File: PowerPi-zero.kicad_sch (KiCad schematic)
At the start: 34 parts, among them J1 2444, J3 Conn_01x02, J6 Raspberry_Pi_2_3, J8 2444, Q1 30V 4A 44mΩ, Q2 50nA 150V 200mW 200mA, Q3 30V 4A 44mΩ, U1 XL4015

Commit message: Layout complete for PowerPi zero
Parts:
- removed D2: SS54, Diode_SMD:D_SMA, symbol Device:D_Schottky
- removed H5, H6, H7, H8: MountingHole, MountingHole:MountingHole_3.5mm, symbol Mechanical:MountingHole
- removed J3: Conn_01x02, Connector_JST:JST_XH_B2B-XH-A_1x02_P2.50mm_Vertical, symbol Connector_Generic:Conn_01x02
- removed JP1: SolderJumper_3_Bridged12, Jumper:SolderJumper-3_P1.3mm_Bridged2Bar12_RoundedPad1.0x1.5mm, symbol Jumper:SolderJumper_3_Bridged12

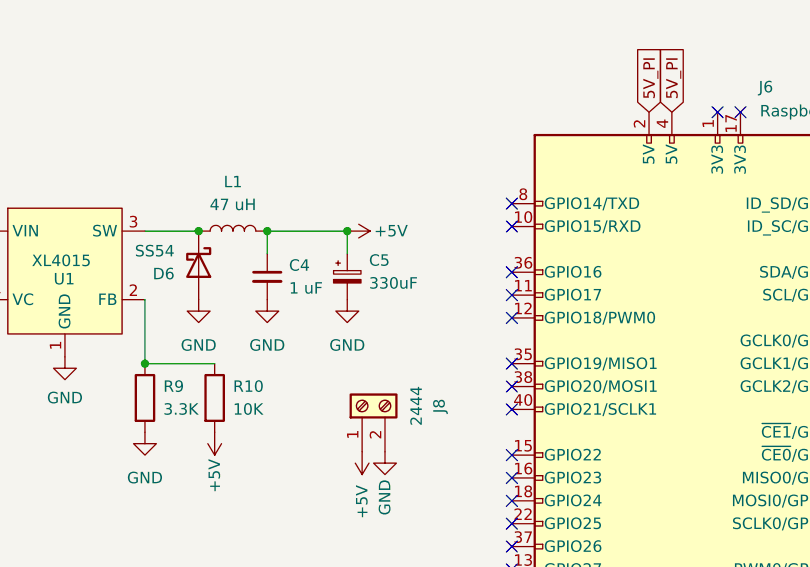
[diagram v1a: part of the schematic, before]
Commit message: update to 1000 uF output electrolytic capacitor
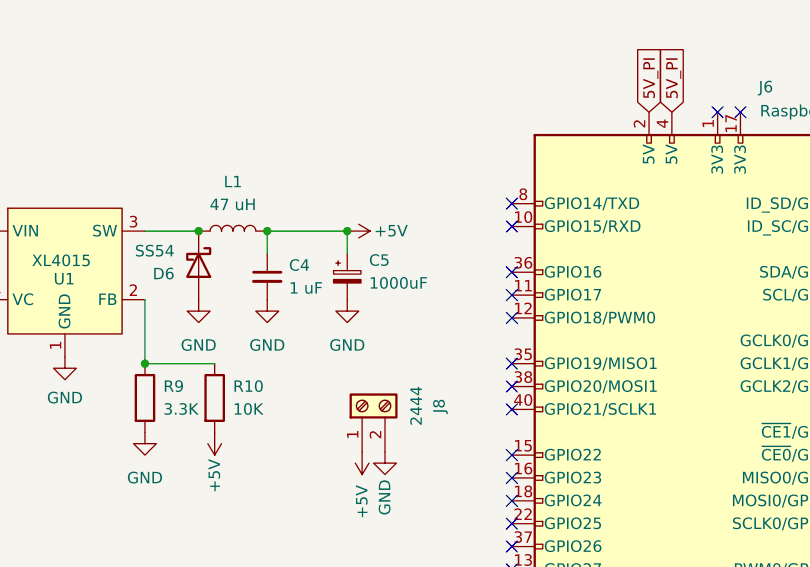
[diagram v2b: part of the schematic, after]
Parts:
- C5: value 330uF -> 1000uF; footprint Capacitor_SMD:CP_Elec_6.3x7.7 -> Capacitor_SMD:CP_Elec_8x10; LCSC C58277 -> C310838; ManfNum RVT1A331M0607 -> RVE1A102M0810; PCBway RVT1A331M0607 -> RVE1A102M0810; abv.Footprint SMD_6.3x7.7mm -> SMD_ECAP-8x10
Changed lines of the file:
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@@
       (effects (font (size 1.27 1.27)) (justify left))
     )
-    (property "Value" "330uF" (id 1) (at 126.111 101.4348 0)
-      (effects (font (size 1.27 1.27)) (justify left))
-    )
-    (property "Footprint" "Capacitor_SMD:CP_Elec_6.3x7.7" (id 2) (at 123.698 100.711 0)
+    (property "Value" "1000uF" (id 1) (at 126.111 101.4348 0)
+      (effects (font (size 1.27 1.27)) (justify left))
+    )
+    (property "Footprint" "Capacitor_SMD:CP_Elec_8x10" (id 2) (at 123.698 100.711 0)
       (effects (font (size 1.27 1.27)) hide)
     )
@@
       (effects (font (size 1.27 1.27)) hide)
     )
-    (property "LCSC" "C58277" (id 4) (at 123.698 100.711 0)
-      (effects (font (size 1.27 1.27)) hide)
-    )
-    (property "PCBway" "RVT1A331M0607" (id 5) (at 123.698 100.711 0)
-      (effects (font (size 1.27 1.27)) hide)
-    )
-    (property "abv.Footprint" "SMD_6.3x7.7mm" (id 6) (at 123.698 100.711 0)
-      (effects (font (size 1.27 1.27)) hide)
-    )
-    (property "ManfNum" "RVT1A331M0607" (id 7) (at 123.698 100.711 0)
+    (property "LCSC" "C310838" (id 4) (at 123.698 100.711 0)
+      (effects (font (size 1.27 1.27)) hide)
+    )
+    (property "PCBway" "RVE1A102M0810" (id 5) (at 123.698 100.711 0)
+      (effects (font (size 1.27 1.27)) hide)
+    )
+    (property "abv.Footprint" "SMD_ECAP-8x10" (id 6) (at 123.698 100.711 0)
+      (effects (font (size 1.27 1.27)) hide)
+    )
+    (property "ManfNum" "RVE1A102M0810" (id 7) (at 123.698 100.711 0)
       (effects (font (size 1.27 1.27)) hide)
     )
@@
     )
     (path "/858d080d-4b19-45cc-bb9f-d3c272f2a854"
-      (reference "C5") (unit 1) (value "330uF") (footprint "Capacitor_SMD:CP_Elec_6.3x7.7")
+      (reference "C5") (unit 1) (value "1000uF") (footprint "Capacitor_SMD:CP_Elec_8x10")
     )
     (path "/09682f05-b4e6-4e50-98a0-ce1e14e1d9ed"

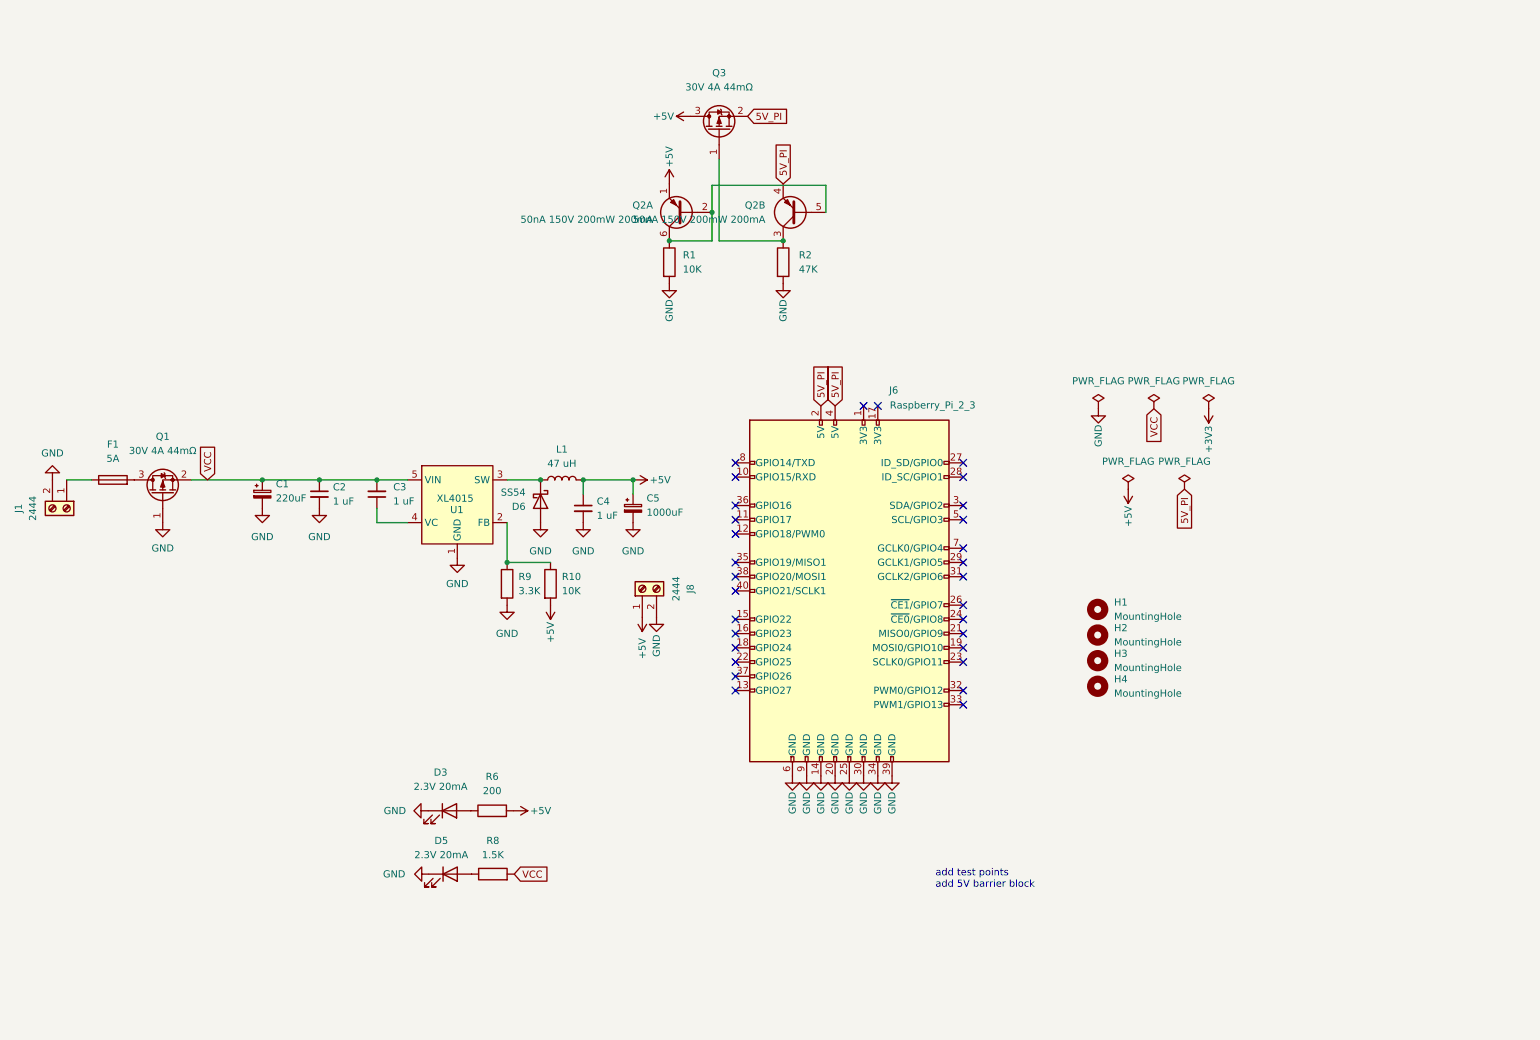
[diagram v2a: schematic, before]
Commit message: Brought full design up to date with ElectriPi
Main development was done on ElectriPi so now ElectriPi mini matches those developments
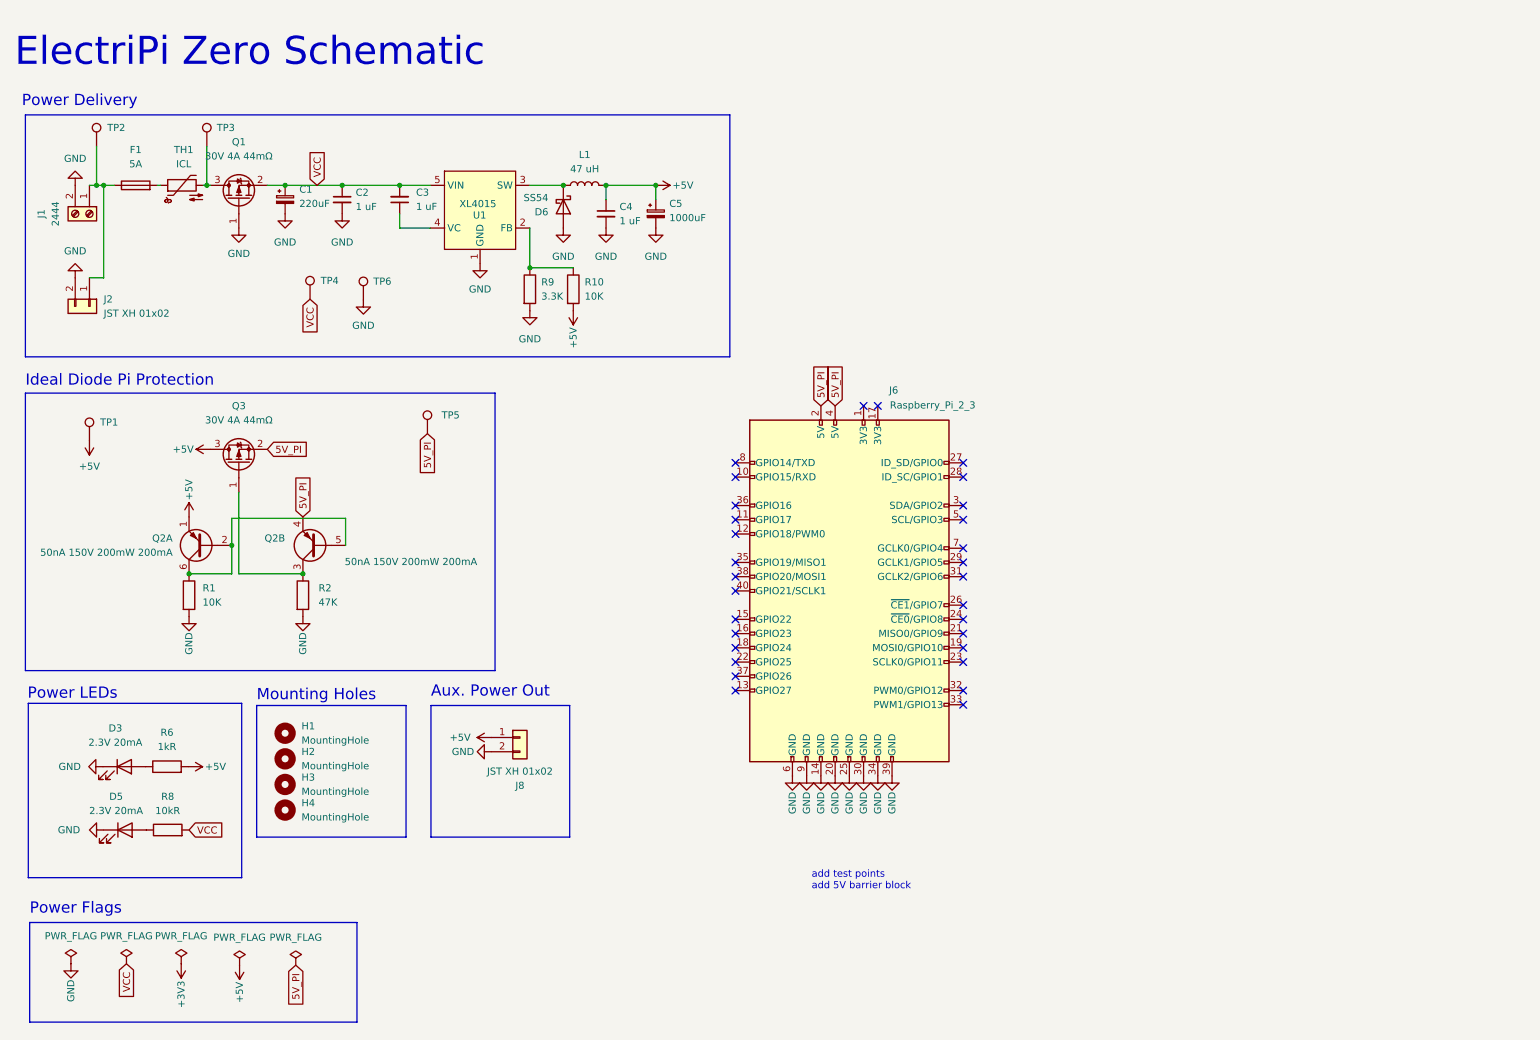
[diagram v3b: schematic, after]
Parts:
- added J2: JST XH 01x02, Connector_JST:JST_XH_B2B-XH-A_1x02_P2.50mm_Vertical, symbol Connector_Generic:Conn_01x02
- added TH1: ICL, Inrush_Limiter:5_OR_7pt5_PITCH_ICL, symbol Device:Thermistor_NTC
- added TP1, TP2, TP3, TP4, TP5, TP6: TestPoint, TestPoint:TestPoint_Pad_D1.5mm, symbol Connector:TestPoint
- F1: footprint Fuse:Fuseholder_Blade_Mini_Keystone_3568 -> Fuse:Fuse_Littelfuse-NANO2-451_453; LCSC (none) -> C108518
- J8: value 2444 -> JST XH 01x02; symbol Connector:Screw_Terminal_01x02 -> Connector_Generic:Conn_01x02; LCSC (none) -> C492456; now in the parts list
- R6: value 200 -> 1kR
- R8: value 1.5K -> 10kR
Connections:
- net +5V: now also TP1.1
- net 5V_PI: now also TP5.1
- net GND: now also J2.2 (Pin_2), TP6.1
- net VCC: now also TP4.1
- net at F1.1, J1.1 (Pin_1): now also J2.1 (Pin_1), TP2.1
- net at Q1.3 (D): now also TH1.2, TP3.1; no longer F1.2
- new net: F1.2, TH1.1
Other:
- note added: "Aux. Power Out"
- note added: "ElectriPi Zero Schematic"
- note added: "Ideal Diode Pi Protection"
- note added: "Mounting Holes"
- note added: "Power Delivery"
- note added: "Power Flags"
- note added: "Power LEDs"
- moved on the sheet: C1, C2, C3, C4, C5, D3, D5, D6, F1, H1, H2, H3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

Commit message: Upgrade to TI part, matching ElectriPi.
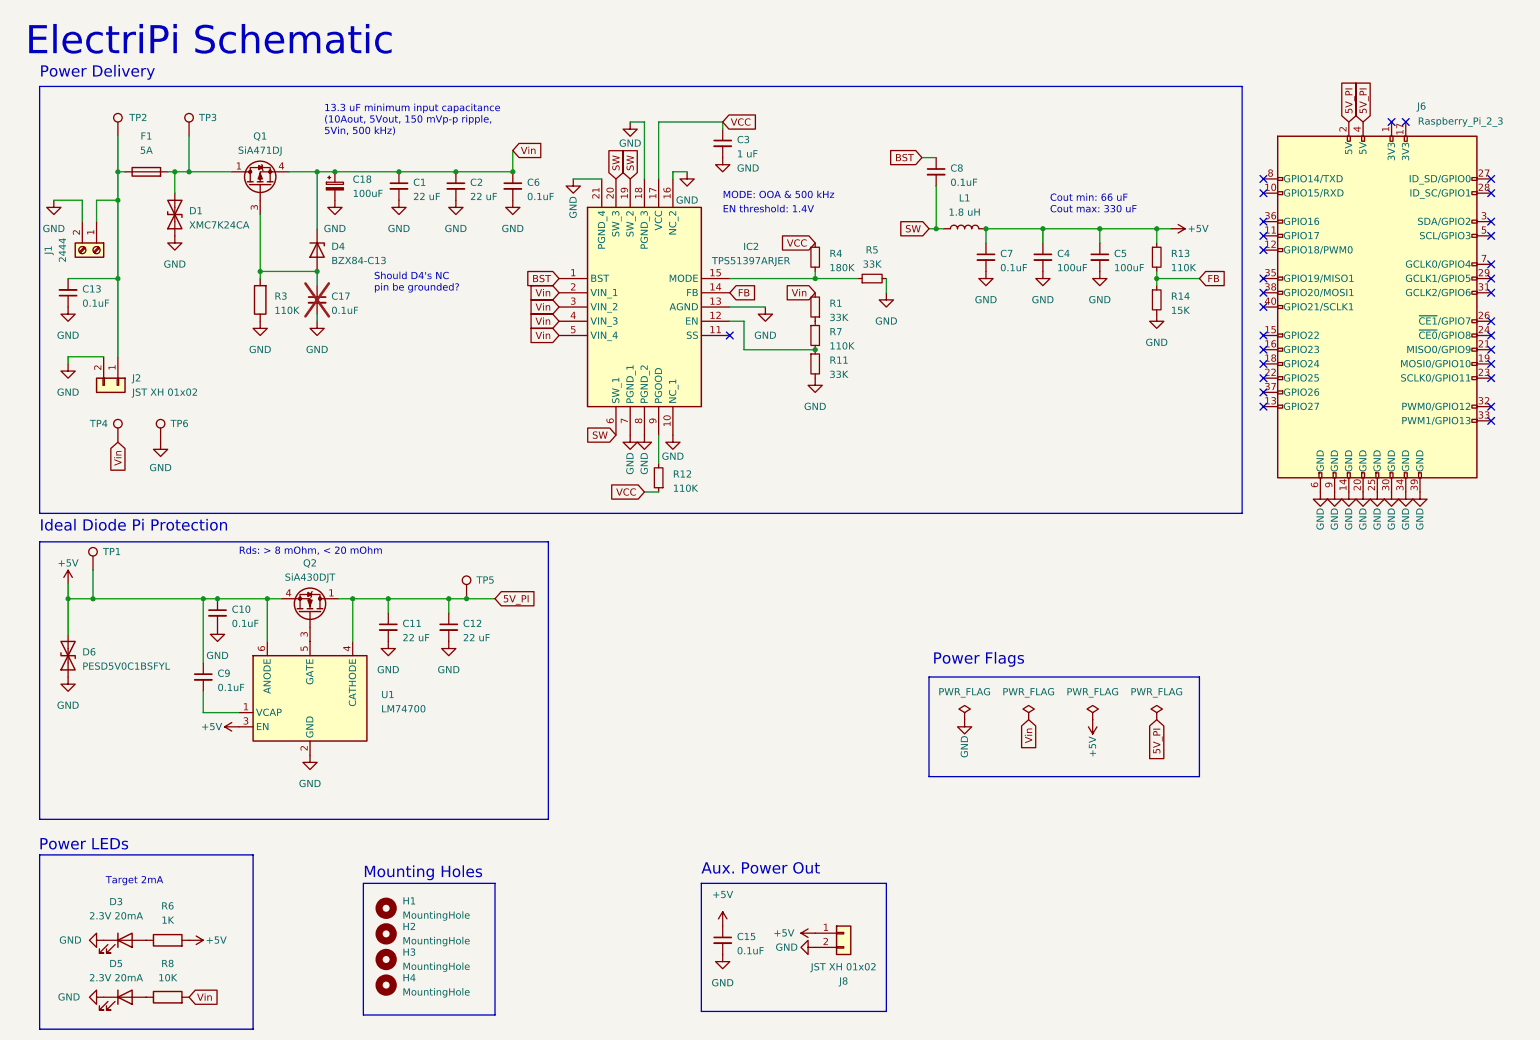
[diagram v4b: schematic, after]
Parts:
- removed C1: 220uF, Capacitor_SMD:CP_Elec_10x10, symbol Device:C_Polarized_Small
- removed C5: 1000uF, Capacitor_SMD:CP_Elec_8x10, symbol Device:C_Polarized_Small
- removed D6: SS54, Diode_SMD:D_SMA, symbol Device:D_Schottky
- removed Q1, Q3: 30V 4A 44mΩ, Package_TO_SOT_SMD:SOT-23, symbol Transistor_FET:AO3401A
- removed Q2: 50nA 150V 200mW 200mA, Package_TO_SOT_SMD:SOT-363_SC-70-6, symbol Transistor_BJT:MMDT5401
- removed R1: 10K, Resistor_SMD:R_0402_1005Metric, symbol Device:R
- removed R10: 10K, Resistor_SMD:R_0603_1608Metric, symbol Device:R
- removed R2: 47K, Resistor_SMD:R_0402_1005Metric, symbol Device:R
- removed R9: 3.3K, Resistor_SMD:R_0603_1608Metric, symbol Device:R
- removed TH1: ICL, Inrush_Limiter:5_OR_7pt5_PITCH_ICL, symbol Device:Thermistor_NTC
- removed U1: XL4015, Package_TO_SOT_SMD:TO-263-5_TabPin3, symbol Regulator_Switching:XL4015
- added C1, C11, C12: 22 uF, Capacitor_SMD:C_0805_2012Metric, symbol Device:C_Small
- added C10, C13, C15, C17, C6, C7, C8, C9: 0.1uF, Capacitor_SMD:C_0402_1005Metric, symbol Device:C_Small
- added C18: 100uF, Capacitor_SMD:CP_Elec_8x10, symbol Device:C_Polarized_Small
- added C5: 100uF, Capacitor_SMD:C_1206_3216Metric, symbol Device:C_Small
- added D1: XMC7K24CA, Diode_SMD:D_SMC, symbol Device:D_TVS
- added D4: BZX84-C13, Package_TO_SOT_SMD:SOT-23, symbol Diode:BZX84Cxx
- added D6: PESD5V0C1BSFYL, Diode_SMD:Nexperia_DSN0603-2_0.6x0.3mm_P0.4mm, symbol Device:D_TVS
- added IC2: TPS51397ARJER, Package_DFN_QFN:QFN-20-1EP_3x3mm_P0.45mm_EP1.6x1.6mm_ThermalVias, symbol TPS51397ARJER:TPS51397ARJER
- added Q1: SiA471DJ, Package_TO_SOT_SMD:Vishay_PowerPAK_SC70-6L_Single, symbol Transistor_FET:SiA449DJ
- added Q2: SiA430DJT, Package_TO_SOT_SMD:Vishay_PowerPAK_SC70-6L_Single, symbol Transistor_FET:SiA430DJT
- added R1, R11, R5: 33K, Resistor_SMD:R_0402_1005Metric, symbol Device:R_Small
- added R12, R13, R7: 110K, Resistor_SMD:R_0402_1005Metric, symbol Device:R_Small
- added R14: 15K, Resistor_SMD:R_0402_1005Metric, symbol Device:R_Small
- added R3: 110K, Resistor_SMD:R_0402_1005Metric, symbol Device:R
- added R4: 180K, Resistor_SMD:R_0402_1005Metric, symbol Device:R_Small
- added U1: LM74700, Package_TO_SOT_SMD:SOT-23-6, symbol Power_Management:LM74700
- C2: value 1 uF -> 22 uF; footprint Capacitor_SMD:C_0603_1608Metric -> Capacitor_SMD:C_0805_2012Metric; LCSC C15849 -> C2179409; ManfNum CL10A105KB8NNNC -> (none); Mouser (none) -> 810-C2012X5R1V226MAC; PCBway CL10A105KB8NNNC -> (none); abv.Footprint 0603 -> (none)
- C4: value 1 uF -> 100uF; footprint Capacitor_SMD:C_0603_1608Metric -> Capacitor_SMD:C_1206_3216Metric; LCSC C15849 -> C312983; ManfNum CL10A105KB8NNNC -> (none); Mouser (none) -> 81-GRM31CR61A107MA8L; PCBway CL10A105KB8NNNC -> (none); abv.Footprint 0603 -> (none)
- F1: ManfNum 0154005.DR -> (none); abv.Footprint SMD-2_5.03x9.73x3.81 -> (none)
- J1: LCSC (none) -> C123214
- J2, J8: LCSC C492456 -> C24193
- L1: value 47 uH -> 1.8 uH; footprint Inductor_SMD:L_12x12mm_H6mm -> Inductor_SMD:L_Vishay_IHLP-4040; LCSC C497913 -> C506636; ManfNum YSPI1365-470M -> (none); Mouser (none) -> 70-IHLP4040DZER1R8M1; PCBway YSPI1365-470M -> (none); abv.Footprint 12x12 -> (none)
- R6: value 1kR -> 1K; LCSC C25087 -> C409028
- R8: value 10kR -> 10K; LCSC C25867 -> C270371
- TP1, TP2, TP3, TP4, TP5, TP6: now left out of the parts list
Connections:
- net +5V: now also C10.1, C15.1, C5.1, C7.1, C9.1, D6.2 (A2), Q2.4 (S), R13.1, U1.3 (EN), U1.6 (ANODE)
- net 5V_PI: now also C11.1, C12.1, Q2.1 (D), U1.4 (CATHODE)
- net GND: now also C3.2, C1.2, C10.2, C11.2, C12.2, C13.1, C15.2, C17.2, C18.2, C5.2, C6.2, C7.2, D1.1 (A1), D6.1 (A1), IC2.10 (NC_1), IC2.13 (AGND), IC2.16 (NC_2), IC2.18 (PGND_3), IC2.21 (PGND_4), IC2.7 (PGND_1), IC2.8 (PGND_2), R11.2, R14.2, R3.1, R5.2, U1.2 (GND)
- net VCC: now also C3.1, IC2.17 (VCC), R12.1, R4.1; no longer C2.1, C3.2, R8.2, TP4.1
- net at F1.1, J1.1 (Pin_1), J2.1 (Pin_1)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: now also C13.2
- net at TP3.1: now also F1.2, D1.2 (A2), Q1.1 (D)
- net SW: now reaches L1.1
- net SW: now also C8.2, IC2.19 (SW_2), IC2.20 (SW_3), IC2.6 (SW_1)
- new net: IC2.12 (EN), R11.1, R7.2
- new net: IC2.15 (MODE), R4.2, R5.1
- new net: IC2.9 (PGOOD), R12.2
- new net: C17.1, D4.1 (A), Q1.3 (G), R3.2
- new net: R1.1, R7.1
- new net: C9.2, U1.1 (VCAP)
- new net: Q2.3 (G), U1.5 (GATE)
- new net BST: C8.1, IC2.1 (BST)
- new net FB: IC2.14 (FB), R13.2, R14.1
- new net Vin: C1.1, C18.1, C2.1, C6.1, D4.3 (K), IC2.2 (VIN_1), IC2.3 (VIN_2), IC2.4 (VIN_3), IC2.5 (VIN_4), Q1.4 (S), R1.2, R8.2, TP4.1
- no-connect marks 30 -> 31
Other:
- note added: "13.3 uF minimum input capacitance (10Aout, 5Vout, 150 mVp-p ripple, 5Vin, 500 kHz)"
- note added: "Cout min: 66 uF Cout max: 330 uF"
- note added: "EN threshold: 1.4V"
- note added: "ElectriPi Schematic"
- note added: "MODE: OOA & 500 kHz"
- note added: "Rds: > 8 mOhm, < 20 mOhm"
- note added: "Should D4's NC pin be grounded?"
- note added: "Target 2mA"
- note removed: "ElectriPi Zero Schematic"
- note removed: "add test points add 5V barrier block"
- title: (none) -> ElectriPi
- moved on the sheet: C3, D3, D5, F1, H1, H2, H3, H4, J1, J6, J8, L1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
